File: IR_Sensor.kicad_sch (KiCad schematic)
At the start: 31 parts, among them J8 Conn_01x03_Female, Q1 AO3401, Q3 NJL7302L-F3, Q31 Q_NPN_BEC, U12 AE-BME280, U17 OSRB38C9AA

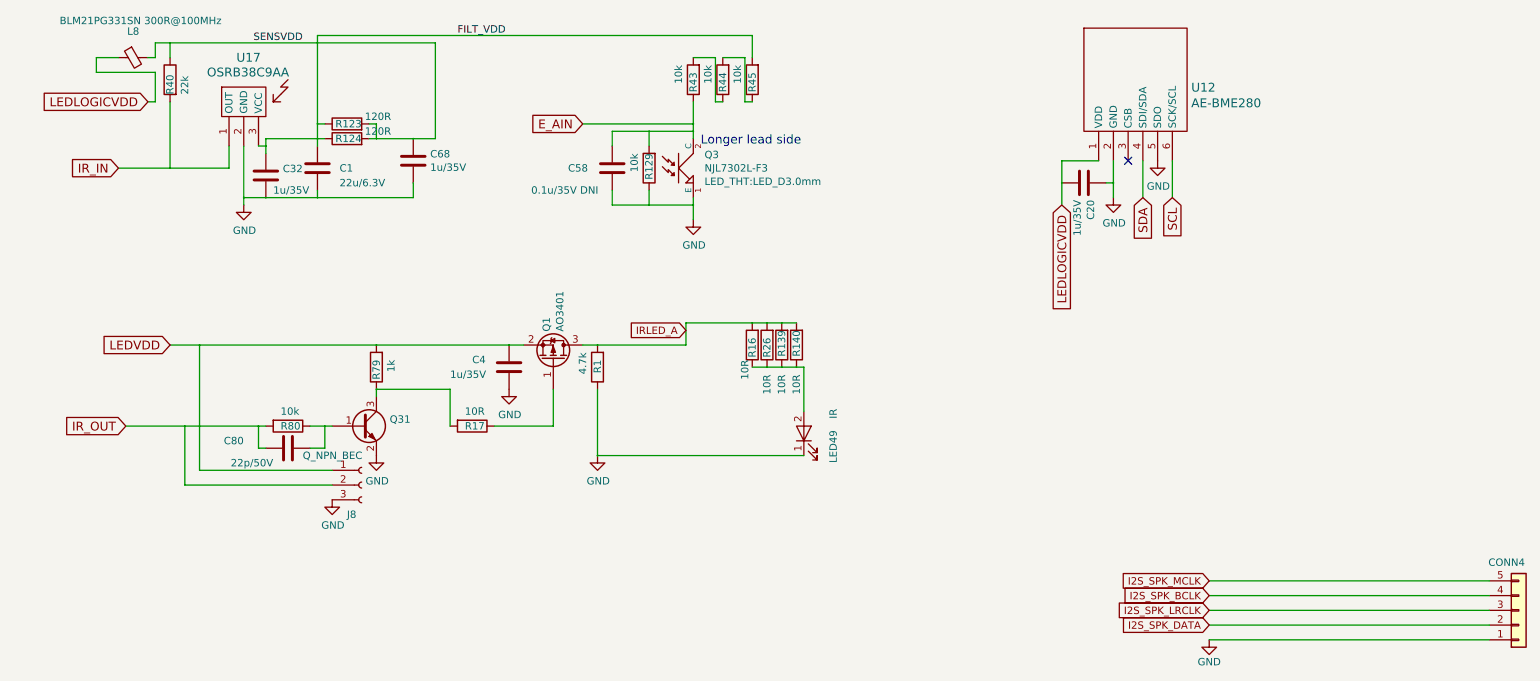
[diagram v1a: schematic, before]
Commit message: Added IR led protection
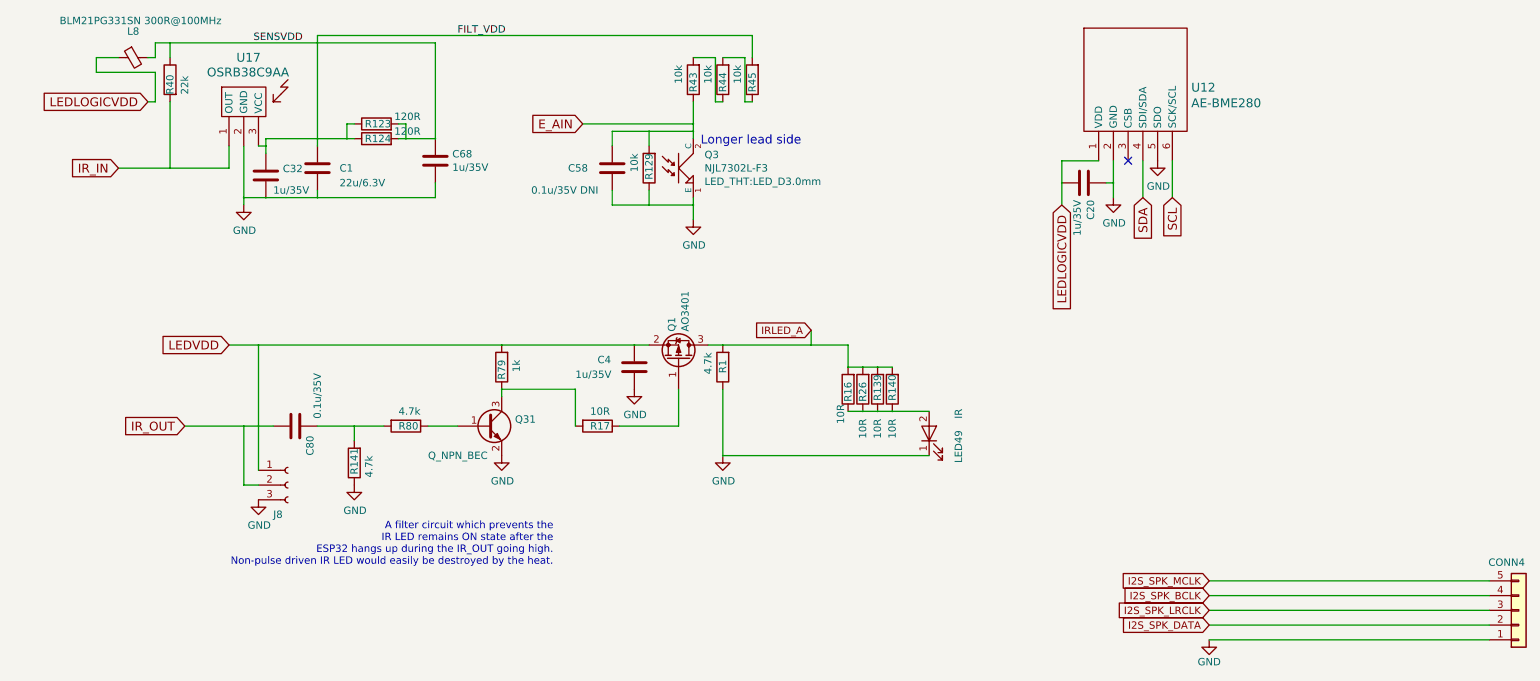
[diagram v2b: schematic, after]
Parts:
- added R141: 4.7k, Resistor_SMD:R_0603_1608Metric_Pad1.05x0.95mm_HandSolder, symbol dotmatrix_64x48-rescue:R-device
- C80: value 22p/50V -> 0.1u/35V
- R80: value 10k -> 4.7k
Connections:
- net GND: now also R141.1
- net IR_OUT: no longer R80.2
- net at Q31.1 (B), R80.1: no longer C80.2
- new net: C80.2, R141.2, R80.2
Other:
- note added: "A filter circuit which prevents the IR LED remains ON state after the ESP32 hangs up during the IR_OUT going high. Non-pulse driven IR LED would easily be destroyed by the heat."
- moved on the sheet: C4, C68, J8, LED49, Q1, Q31, R1, R123, R124, R139, R140, R16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

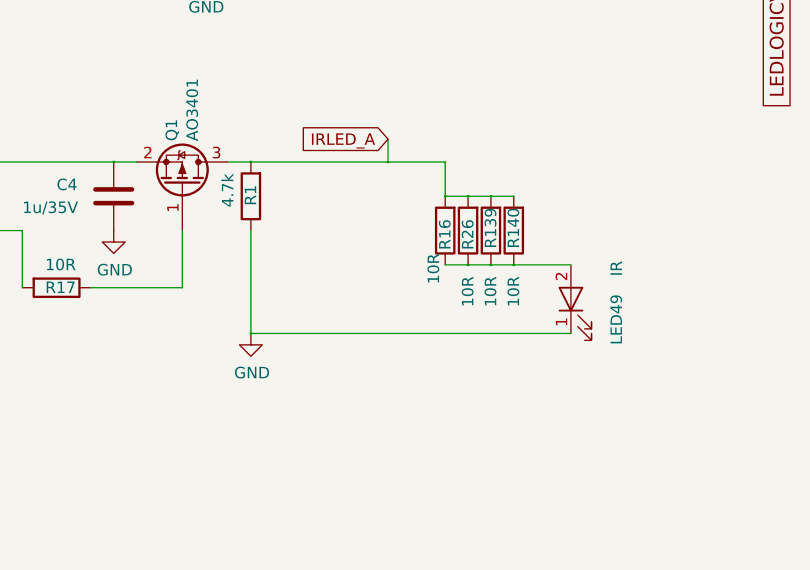
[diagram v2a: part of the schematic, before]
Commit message: Added IR transmit status 'visible' indicator
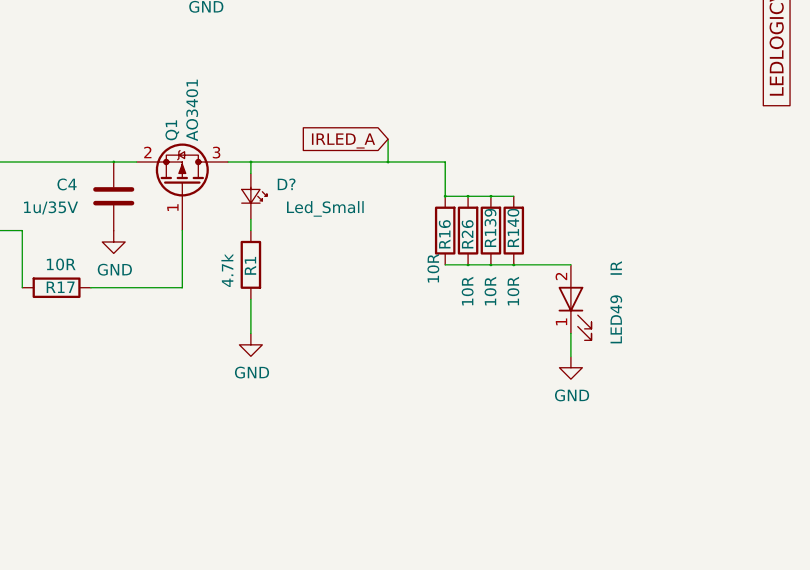
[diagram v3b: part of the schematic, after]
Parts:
- added D?: Led_Small, components:LED1608_Handsoldering, symbol dotmatrix_64x48-rescue:LED_Small-device
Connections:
- net GND: now also R1.2; no longer R1.1
- net IRLED_A: now also D?.2 (A); no longer R1.2
- new net: D?.1 (K), R1.1
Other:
- moved on the sheet: R1
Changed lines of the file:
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@@
   (junction (at 124.46 45.72) (diameter 0.3048) (color 0 0 0 0))
   (junction (at 129.54 69.85) (diameter 0.3048) (color 0 0 0 0))
-  (junction (at 129.54 88.9) (diameter 0.3048) (color 0 0 0 0))
   (junction (at 144.78 69.85) (diameter 0.3048) (color 0 0 0 0))
   (junction (at 151.13 73.66) (diameter 0.3048) (color 0 0 0 0))
@@
     (stroke (width 0) (type solid) (color 0 0 0 0))
   )
-  (wire (pts (xy 129.54 88.9) (xy 129.54 77.47))
-    (stroke (width 0) (type solid) (color 0 0 0 0))
-  )
-  (wire (pts (xy 129.54 88.9) (xy 165.1 88.9))
+  (wire (pts (xy 129.54 69.85) (xy 129.54 71.12))
+    (stroke (width 0) (type solid) (color 0 0 0 0))
+  )
+  (wire (pts (xy 129.54 69.85) (xy 144.78 69.85))
+    (stroke (width 0) (type solid) (color 0 0 0 0))
+  )
+  (wire (pts (xy 129.54 76.2) (xy 129.54 77.47))
+    (stroke (width 0) (type solid) (color 0 0 0 0))
+  )
+  (wire (pts (xy 129.54 88.9) (xy 129.54 85.09))
     (stroke (width 0) (type solid) (color 0 0 0 0))
   )
@@
     (stroke (width 0) (type solid) (color 0 0 0 0))
   )
-  (wire (pts (xy 144.78 69.85) (xy 129.54 69.85))
-    (stroke (width 0) (type solid) (color 0 0 0 0))
-  )
   (wire (pts (xy 151.13 69.85) (xy 144.78 69.85))
     (stroke (width 0) (type solid) (color 0 0 0 0))
@@
   )
   (wire (pts (xy 158.75 81.28) (xy 165.1 81.28))
+    (stroke (width 0) (type solid) (color 0 0 0 0))
+  )
+  (wire (pts (xy 165.1 88.9) (xy 165.1 91.44))
     (stroke (width 0) (type solid) (color 0 0 0 0))
   )
@@
     (property "Datasheet" "" (id 3) (at 129.54 88.9 0))
   )
+  (symbol (lib_id "dotmatrix_64x48-rescue:GND-power") (at 165.1 91.44 0) (unit 1)
+    (in_bom yes) (on_board yes)
+    (property "Reference" "#PWR?" (id 0) (at 165.1 97.79 0)
+      (effects (font (size 1.27 1.27)) hide)
+    )
+    (property "Value" "GND" (id 1) (at 165.227 95.8342 0))
+    (property "Footprint" "" (id 2) (at 165.1 91.44 0))
+    (property "Datasheet" "" (id 3) (at 165.1 91.44 0))
+  )
   (symbol (lib_id "dotmatrix_64x48-rescue:GND-power") (at 196.85 44.45 0) (unit 1)
     (in_bom yes) (on_board yes)
@@
     (property "Datasheet" "" (id 3) (at 213.36 120.65 0))
   )
+  (symbol (lib_id "dotmatrix_64x48-rescue:LED_Small-device") (at 129.54 73.66 270) (mirror x) (unit 1)
+    (in_bom yes) (on_board yes)
+    (property "Reference" "D?" (id 0) (at 134.62 72.39 90)
+      (effects (font (size 1.27 1.27)) (justify right))
+    )
+    (property "Value" "Led_Small" (id 1) (at 142.24 74.93 90)
+      (effects (font (size 1.27 1.27)) (justify right))
+    )
+    (property "Footprint" "components:LED1608_Handsoldering" (id 2) (at 129.54 73.66 90)
+      (effects (font (size 1.27 1.27)) hide)
+    )
+    (property "Datasheet" "" (id 3) (at 129.54 73.66 90))
+  )
   (symbol (lib_id "dotmatrix_64x48-rescue:R-device") (at 34.29 24.13 0) (mirror y) (unit 1)
     (in_bom yes) (on_board yes)
@@
     (property "Datasheet" "" (id 3) (at 129.54 24.13 0))
   )
-  (symbol (lib_id "dotmatrix_64x48-rescue:R-device") (at 129.54 73.66 180) (unit 1)
-    (in_bom yes) (on_board yes)
-    (property "Reference" "R1" (id 0) (at 129.54 72.39 90)
-      (effects (font (size 1.27 1.27)) (justify left))
-    )
-    (property "Value" "4.7k" (id 1) (at 127 71.12 90)
-      (effects (font (size 1.27 1.27)) (justify left))
-    )
-    (property "Footprint" "Resistor_SMD:R_0603_1608Metric_Pad1.05x0.95mm_HandSolder" (id 2) (at 131.318 73.66 90)
-      (effects (font (size 1.27 1.27)) hide)
-    )
-    (property "Datasheet" "" (id 3) (at 129.54 73.66 0))
+  (symbol (lib_id "dotmatrix_64x48-rescue:R-device") (at 129.54 81.28 0) (mirror y) (unit 1)
+    (in_bom yes) (on_board yes)
+    (property "Reference" "R1" (id 0) (at 129.54 82.55 90)
+      (effects (font (size 1.27 1.27)) (justify left))
+    )
+    (property "Value" "4.7k" (id 1) (at 127 83.82 90)
+      (effects (font (size 1.27 1.27)) (justify left))
+    )
+    (property "Footprint" "Resistor_SMD:R_0603_1608Metric_Pad1.05x0.95mm_HandSolder" (id 2) (at 131.318 81.28 90)
+      (effects (font (size 1.27 1.27)) hide)
+    )
+    (property "Datasheet" "" (id 3) (at 129.54 81.28 0))
   )
   (symbol (lib_id "dotmatrix_64x48-rescue:R-device") (at 134.62 24.13 180) (unit 1)

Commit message: Small improvements
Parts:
- gave numbers to parts that had none: 1
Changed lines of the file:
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@@
   (symbol (lib_id "dotmatrix_64x48-rescue:GND-power") (at 165.1 91.44 0) (unit 1)
     (in_bom yes) (on_board yes)
-    (property "Reference" "#PWR?" (id 0) (at 165.1 97.79 0)
+    (property "Reference" "#PWR0155" (id 0) (at 165.1 97.79 0)
       (effects (font (size 1.27 1.27)) hide)
     )
@@
   (symbol (lib_id "dotmatrix_64x48-rescue:LED_Small-device") (at 129.54 73.66 270) (mirror x) (unit 1)
     (in_bom yes) (on_board yes)
-    (property "Reference" "D?" (id 0) (at 134.62 72.39 90)
+    (property "Reference" "D10" (id 0) (at 134.62 72.39 90)
       (effects (font (size 1.27 1.27)) (justify right))
     )

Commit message: Added some comments
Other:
- note added: "Note: LEDVDD *may* higher than IR_OUT logic. This will always drive Q1 as on state."
- note added: "Use AE-BME280 as I2C mode."
- note added: "You will see this stupid low-pass filter on the VCC line in some IR receiver chip datasheet. I don't know why they are so much volunerable to the power noise."
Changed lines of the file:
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@@
-(kicad_sch (version 20200820) (host eeschema "5.99.0-unknown-b0af66afc~103~ubuntu18.04.1")
+(kicad_sch (version 20200827) (generator eeschema)
   (page 2 10)
   (paper "A4")
@@
     (stroke (width 0) (type solid) (color 0 0 0 0))
   )
+  (text "You will see this stupid low-pass filter on the VCC line in\nsome IR receiver chip datasheet. I don't know why they\nare so much volunerable to the power noise."
+    (at 78.74 58.42 0)
+    (effects (font (size 1.27 1.27)) (justify right bottom))
+  )
   (text "A filter circuit which prevents the\nIR LED remains ON state after the\nESP32 hangs up during the IR_OUT going high.\nNon-pulse driven IR LED would easily be destroyed by the heat."
     (at 100.33 107.95 0)
@@
     (effects (font (size 1.524 1.524)) (justify left bottom))
   )
+  (text "Note: LEDVDD *may* higher than IR_OUT logic.\nThis will always drive Q1 as on state."
+    (at 154.94 101.6 0)
+    (effects (font (size 1.27 1.27)) (justify right bottom))
+  )
+  (text "Use AE-BME280 as I2C mode." (at 228.6 58.42 180)
+    (effects (font (size 1.27 1.27)) (justify right bottom))
+  )
   (label "SENSVDD" (at 57.15 17.78 180)

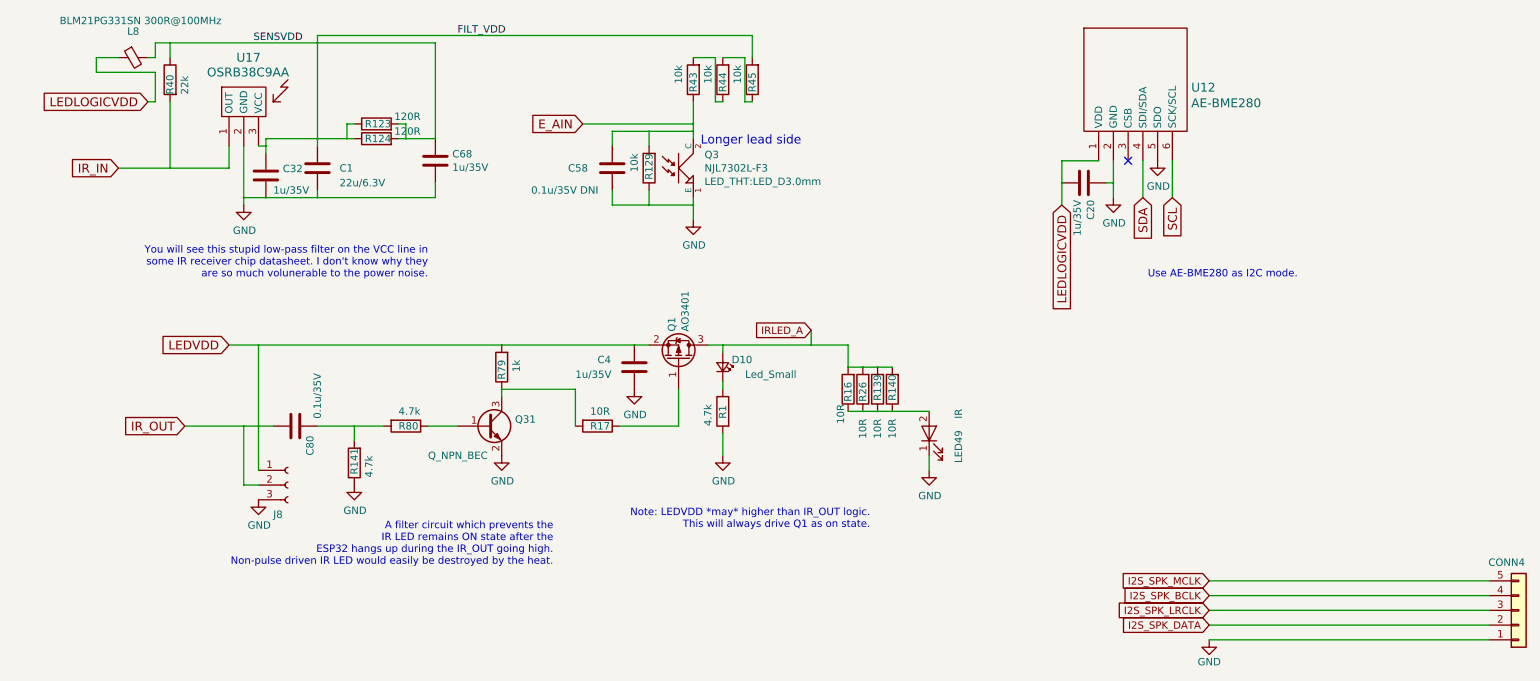
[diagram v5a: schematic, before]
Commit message: Fixed some comments; Added FB on SCL/SDA line
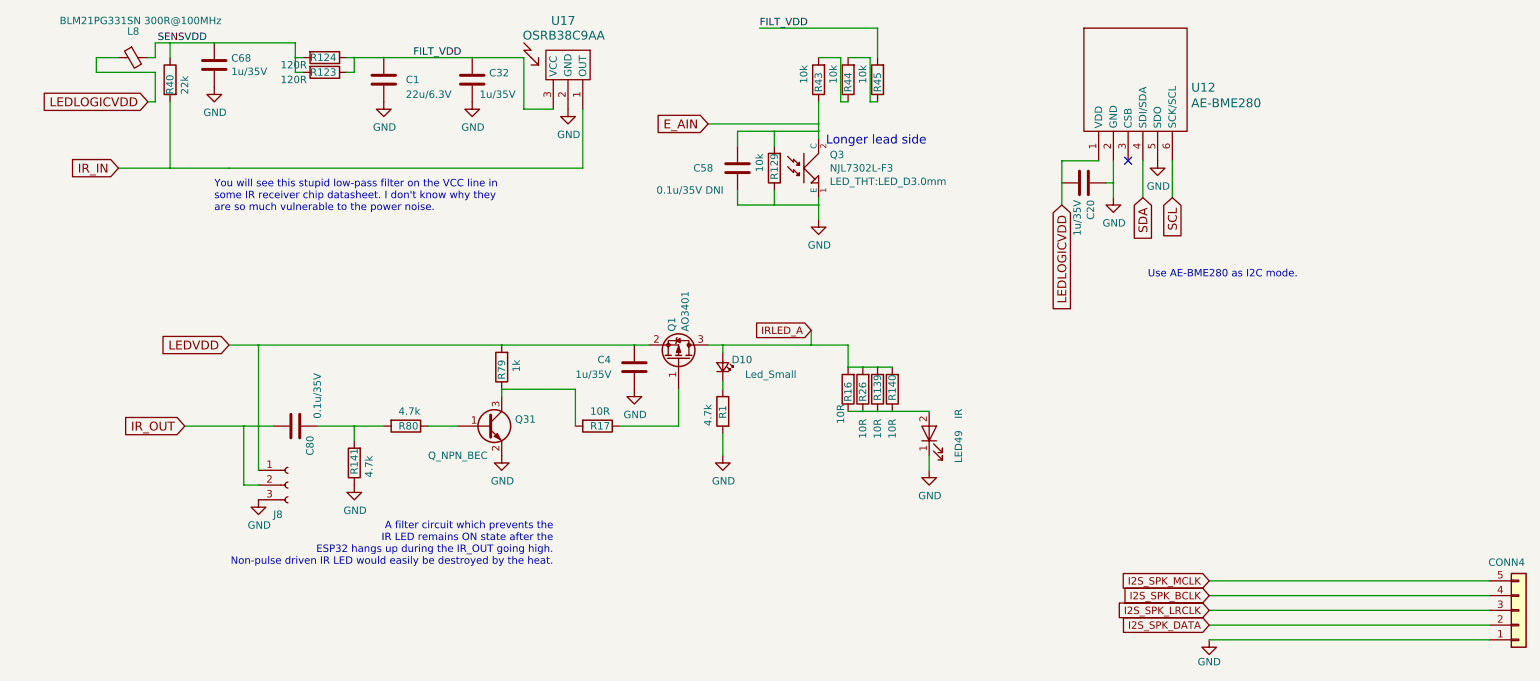
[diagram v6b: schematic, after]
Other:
- note added: "You will see this stupid low-pass filter on the VCC line in some IR receiver chip datasheet. I don't know why they are so much vulnerable to the power noise."
- note removed: "Note: LEDVDD *may* higher than IR_OUT logic. This will always drive Q1 as on state."
- note removed: "You will see this stupid low-pass filter on the VCC line in some IR receiver chip datasheet. I don't know why they are so much volunerable to the power noise."
- moved on the sheet: C1, C32, C58, C68, Q3, R123, R124, R129, R43, R44, R45, U17
